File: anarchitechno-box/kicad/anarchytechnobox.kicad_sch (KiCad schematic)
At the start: 19 parts, among them J1 Conn_01x02, Q1 IRLZ44N, Q2 IRFS4310Z, U1 TC4426xOA, U2 ADuM1200AR, U4 LM7812_TO220, U5 L7805, U6 TME-0503S

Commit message: RP2350 initial commit
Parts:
- removed A1: RaspberryPi_Pico_W, Module:RaspberryPi_Pico_W_SMD_HandSolder, symbol MCU_Module:RaspberryPi_Pico_W
- removed D1, D4: D_Schottky, symbol Device:D_Schottky
- removed D2: RED, symbol Device:LED
- removed D5: GREEN, symbol Device:LED
- removed F1: Polyfuse, symbol Device:Polyfuse
- removed J1: Conn_01x02, symbol Connector_Generic:Conn_01x02
- removed Q1: IRLZ44N, Package_TO_SOT_THT:TO-220-3_Vertical, symbol Transistor_FET:IRLZ44N
- removed Q2: IRFS4310Z, Package_TO_SOT_SMD:TO-263-2, symbol Transistor_FET:IRFS4310Z
- removed R1: 2k2, symbol Device:R
- removed R2: 100R, symbol Device:R
- removed R3: 10k, symbol Device:R
- removed R4: 2k2, symbol Device:R_Small
- removed U1: TC4426xOA, Package_SO:SOIC-8_3.9x4.9mm_P1.27mm, symbol Driver_FET:TC4426xOA
- removed U2: ADuM1200AR, Package_SO:SOIC-8_3.9x4.9mm_P1.27mm, symbol Isolator:ADuM1200AR
- added C101, C102: 100nF, Capacitor_SMD:C_0402_1005Metric, symbol TINRS - Wobbler (pico)sch-eagle-import:C-EUC0402
- added D1, D101: C5349953, TinyLEDs:XL-1010, symbol TinyLEDs:XL-1010
- added H11, H12, H5, H7, H8, H9: MountingHole, MountingHole:MountingHole_3.2mm_M3, symbol Mechanical:MountingHole
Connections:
- net GND: now also C101.1, C102.1, D1.3 (GND), D101.3 (GND)
- new net: D1.1 (DO), D101.4 (DI)
- new net +3V3: C101.2, C102.2, D1.2 (VDD), D101.2 (VDD)
- new net LED_STRING: D1.4 (DI)
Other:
- added sheet RP2350BMCU (RP2350BMCU.kicad_sch)
- added sheet TwoIsolatedFETs (TwoIsolatedFETs.kicad_sch)
- added sheet TwoIsolatedFETs1 (TwoIsolatedFETs.kicad_sch)
- added sheet TwoIsolatedFETs2 (TwoIsolatedFETs.kicad_sch)
- added sheet TwoIsolatedFETs3 (TwoIsolatedFETs.kicad_sch)
- note removed: "both footprints possible: Dpak 252 or TO220"

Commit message: Large intermediate schematic push. Remaining todos are on frontpage.
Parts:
- renumbered C101 to C1, C102 to C2, D3 to D1, D1 to D2, D101 to D3, H5 to H1, H9 to H2, H7 to H3, H11 to H4, H12 to H5, H8 to H6, U6 to U1, U5 to U2, U4 to U3
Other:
- sheet TwoIsolatedFETs renamed TwoIsolatedFETs0
- removed sheet TwoIsolatedFETs2
- removed sheet TwoIsolatedFETs3
- added sheet DCDC Flyback (dcdc_flyback.kicad_sch)
- added sheet Ethernet (eth_w5500.kicad_sch)
- added sheet Isolators (isolators.kicad_sch)
- sheet RP2350BMCU ports: added DRV_CS1, DRV_CS2, DRV_CS3, DRV_CS4, DRV_MISO, DRV_MOSI, DRV_SCK, DRV_nFAULT, ETH_CS, ETH_MISO, ETH_MOSI, ETH_SCK, I2C0_SCL, I2C0_SDA, I2C1_SCL, I2C1_SDA, PMW1_A, PWM0_A, PWM10_A, PWM11_A, PWM2_A, PWM3_A, PWM4_A, PWM5_A, PWM6_A, PWM7_A, PWM8_A, PWM9_A, UART0_RX, UART0_TX, UART1_RX, UART1_TX; removed none
- sheet TwoIsolatedFETs0 ports: added DRV_nFAULT_COMMON, MCU_PWM_A_1, MCU_PWM_A_2, MCU_PWM_B_1, MCU_PWM_B_2, OUTPUT_A, OUTPUT_B, OUTPUT_C, OUTPUT_D, PWM_A_OFF, PWM_B_OFF, SPI_CLK, SPI_CS_A, SPI_CS_B, SPI_MISO, SPI_MOSI; removed Input_A, Input_B
- sheet TwoIsolatedFETs1 ports: added DRV_nFAULT_COMMON, MCU_PWM_A_1, MCU_PWM_A_2, MCU_PWM_B_1, MCU_PWM_B_2, OUTPUT_A, OUTPUT_B, OUTPUT_C, OUTPUT_D, PWM_A_OFF, PWM_B_OFF, SPI_CLK, SPI_CS_A, SPI_CS_B, SPI_MISO, SPI_MOSI; removed Input_A, Input_B
- note added: "HIGH POWER SIDE"
- note added: "MCU SIDE"
- note added: "TODO: - Add 3.3V regulator at power side (+3.3VP) - Add off-the-shelf isolated 5V 6W+ DC/DC (e.g. Recom REC10K-2405SAW/H2) - Add LED indicator chain (I moved Rpi pin) - does it need stay isolated? - Check if Pin allocations don't collide (in particular PWMs and SPIs) - MIDI stuff - OLED display connector - Optocoupler inputs - Rotary encoder etc. - Groove connector"
- moved on the sheet: C1, C2, D1, H1, H2, H3, H4, H5, H6, U1, U2, U3

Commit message: Stijn in de Trein
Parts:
- added J3, J4, J5, J6: Screw_Terminal_01x02, TerminalBlock_Phoenix:TerminalBlock_Phoenix_PT-1,5-2-5.0-H_1x02_P5.00mm_Horizontal, symbol Connector:Screw_Terminal_01x02
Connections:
- net TwoIsolatedFETs0/OUTPUT_A: now also J3.1 (Pin_1)
- net TwoIsolatedFETs0/OUTPUT_B: now also J3.2 (Pin_2)
- net TwoIsolatedFETs0/OUTPUT_C: now also J4.1 (Pin_1)
- net TwoIsolatedFETs0/OUTPUT_D: now also J4.2 (Pin_2)
- net TwoIsolatedFETs1/OUTPUT_A: now also J5.1 (Pin_1)
- net TwoIsolatedFETs1/OUTPUT_B: now also J5.2 (Pin_2)
- net TwoIsolatedFETs1/OUTPUT_C: now also J6.1 (Pin_1)
- net TwoIsolatedFETs1/OUTPUT_D: now also J6.2 (Pin_2)

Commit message: meer Stijn in de Trein
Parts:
- added C86, C87, C88, C89, C90, C91: 100nF, Capacitor_SMD:C_0402_1005Metric, symbol TINRS - Wobbler (pico)sch-eagle-import:C-EUC0402
- added D18, D19, D20, D21, D22, D23: C5349953, TinyLEDs:XL-1010, symbol TinyLEDs:XL-1010
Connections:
- net +3V3: now also C86.2, C87.2, C88.2, C89.2, C90.2, C91.2, D18.2 (VDD), D19.2 (VDD), D20.2 (VDD), D21.2 (VDD), D22.2 (VDD), D23.2 (VDD)
- net GND: now also C86.1, C87.1, C88.1, C89.1, C90.1, C91.1, D18.3 (GND), D19.3 (GND), D20.3 (GND), D21.3 (GND), D22.3 (GND), D23.3 (GND)
- net at D3.1 (DO): now also D18.4 (DI)
- net TwoIsolatedFETs0/OUTPUT_A renamed HB_1_OUT_A
- net TwoIsolatedFETs0/OUTPUT_B renamed HB_1_OUT_B
- net TwoIsolatedFETs0/OUTPUT_C renamed HB_1_OUT_C
- net TwoIsolatedFETs0/OUTPUT_D renamed HB_1_OUT_D
- net TwoIsolatedFETs1/OUTPUT_A renamed HB_2_OUT_A
- net TwoIsolatedFETs1/OUTPUT_B renamed HB_2_OUT_B
- net TwoIsolatedFETs1/OUTPUT_C renamed HB_2_OUT_C
- net TwoIsolatedFETs1/OUTPUT_D renamed HB_2_OUT_D
- new net: D22.1 (DO), D23.4 (DI)
- new net: D21.1 (DO), D22.4 (DI)
- new net: D20.1 (DO), D21.4 (DI)
- new net: D18.1 (DO), D19.4 (DI)
- new net: D19.1 (DO), D20.4 (DI)
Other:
- moved on the sheet: J3, J4, J5, J6

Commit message: nog meer trein
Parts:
- removed J3, J4, J5, J6: Screw_Terminal_01x02, TerminalBlock_Phoenix:TerminalBlock_Phoenix_PT-1,5-2-5.0-H_1x02_P5.00mm_Horizontal, symbol Connector:Screw_Terminal_01x02
- added J3, J4, J5, J6: Screw_Terminal_01x03, TerminalBlock_Phoenix:TerminalBlock_Phoenix_MKDS-1,5-3-5.08_1x03_P5.08mm_Horizontal, symbol Connector:Screw_Terminal_01x03
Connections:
- net GND2: now also J3.2 (Pin_2), J4.2 (Pin_2), J5.2 (Pin_2), J6.2 (Pin_2)
- net HB_1_OUT_A: now also J3.1 (Pin_1)
- net HB_1_OUT_B: now also J3.3 (Pin_3)
- net HB_1_OUT_C: now also J4.1 (Pin_1)
- net HB_1_OUT_D: now also J4.3 (Pin_3)
- net HB_2_OUT_A: now also J5.1 (Pin_1)
- net HB_2_OUT_B: now also J5.3 (Pin_3)
- net HB_2_OUT_C: now also J6.1 (Pin_1)
- net HB_2_OUT_D: now also J6.3 (Pin_3)

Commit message: trein trein trein
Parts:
- removed D1: SM6T24A, Diode_SMD:D_SMB, symbol Diode:SM6T24A
- removed U1: TME-0503S, Converter_DCDC:Converter_DCDC_TRACO_TME_03xxS_05xxS_12xxS_Single_THT, symbol Converter_DCDC:TME-0503S
- removed U2: L7805, symbol Regulator_Linear:L7805
- removed U3: LM7812_TO220, Package_TO_SOT_THT:TO-220-3_Vertical, symbol Regulator_Linear:LM7812_TO220

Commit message: choo choooooo
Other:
- added sheet RS485 (RS485.kicad_sch)
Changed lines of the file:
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@@
 		)
 	)
+	(wire
+		(pts
+			(xy 91.44 88.9) (xy 99.06 88.9)
+		)
+		(stroke
+			(width 0)
+			(type default)
+		)
+	)
 	(polyline
 		(pts
@@
 	(wire
 		(pts
+			(xy 91.44 86.36) (xy 99.06 86.36)
+		)
+		(stroke
+			(width 0)
+			(type default)
+		)
+	)
+	(wire
+		(pts
 			(xy 238.76 123.19) (xy 294.64 123.19)
 		)
@@
 				)
 			)
+		)
+	)
+	(sheet
+		(at 69.85 78.74)
+		(size 21.59 12.7)
+		(exclude_from_sim no)
+		(in_bom yes)
+		(on_board yes)
+		(dnp no)
+		(fields_autoplaced yes)
+		(stroke
+			(width 0.1524)
+			(type solid)
+		)
+		(fill
+			(color 0 0 0 0.0000)
+		)
+		(property "Sheetname" "RS485"
+			(at 69.85 78.0284 0)
+			(effects
+				(font
+					(size 1.27 1.27)
+				)
+				(justify left bottom)
+			)
+		)
+		(property "Sheetfile" "RS485.kicad_sch"
+			(at 69.85 92.0246 0)
+			(effects
+				(font
+					(size 1.27 1.27)
+				)
+				(justify left top)
+				(hide yes)
+			)
+		)
+		(pin "485_~{RE}" input
+			(at 69.85 82.55 180)
+			(effects
+				(font
+					(size 1.27 1.27)
+				)
+				(justify left)
+			)
+		)
+		(pin "FROM_RS485" output
+			(at 91.44 88.9 0)
+			(effects
+				(font
+					(size 1.27 1.27)
+				)
+				(justify right)
+			)
+		)
+		(pin "485_DE" input
+			(at 69.85 85.09 180)
+			(effects
+				(font
+					(size 1.27 1.27)
+				)
+				(justify left)
+			)
+		)
+		(pin "TO_RS485" input
+			(at 91.44 86.36 0)
+			(effects
+				(font
+					(size 1.27 1.27)
+				)
+				(justify right)
+			)
+		)
+		(instances
+			(project "anarchytechnobox"
+				(path "/8c734c41-38ed-40fc-83bd-134786dcfb35"
+					(page "12")
+				)
+			)

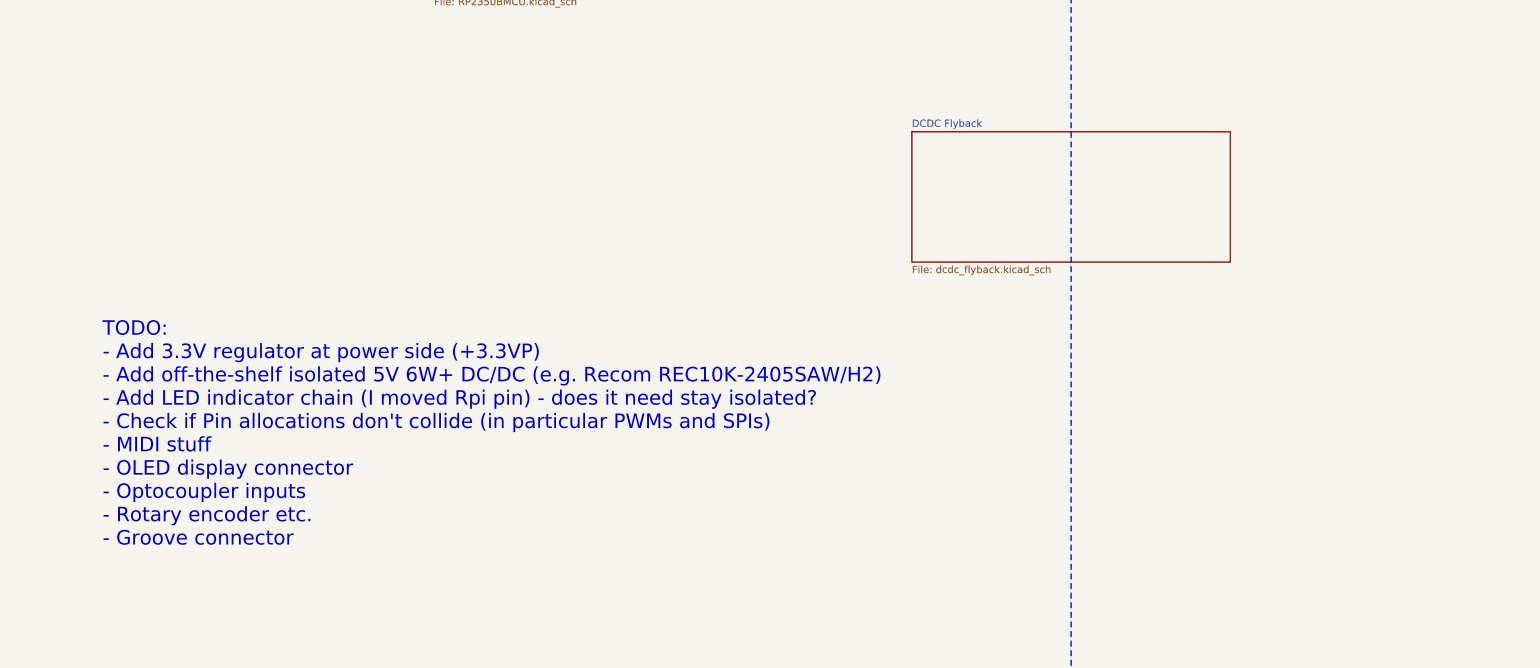
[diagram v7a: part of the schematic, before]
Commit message: Resized PCB with mounts at 125x125mm (suitable for 140mm PC fan), 4-pin fan connector added, changed 3.3VP to 5.0VP
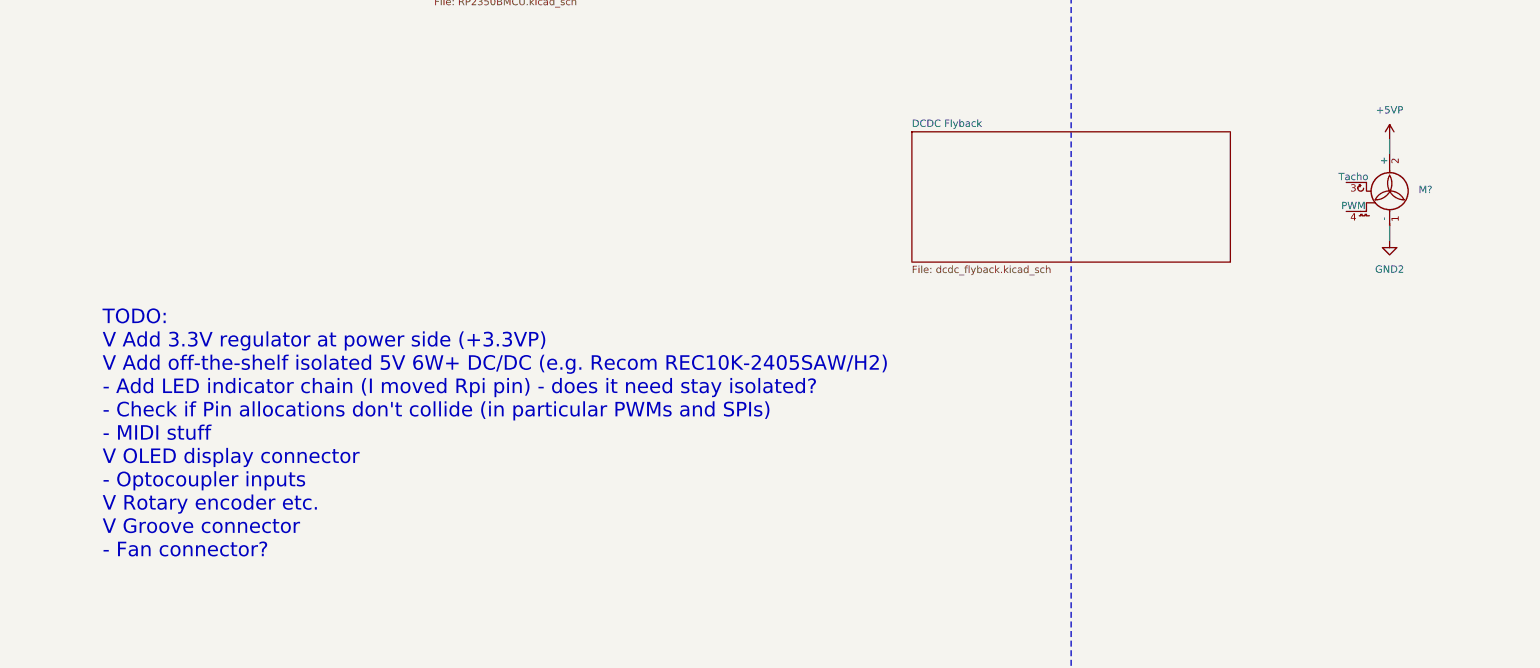
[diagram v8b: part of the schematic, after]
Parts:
- added M?: Fan_Tacho_PWM, Connector:FanPinHeader_1x04_P2.54mm_Vertical, symbol Motor:Fan_Tacho_PWM
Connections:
- net GND2: now also M?.1 (-)
- new net +5VP: M?.2 (+)
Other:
- note added: "TODO: V Add 3.3V regulator at power side (+3.3VP) V Add off-the-shelf isolated 5V 6W+ DC/DC (e.g. Recom REC10K-2405SAW/H2) - Add LED indicator chain (I moved Rpi pin) - does it need stay isolated? - Check if Pin allocations don't collide (in particular PWMs and SPIs) - MIDI stuff V OLED display connector - Optocoupler inputs V Rotary encoder etc. V Groove connector - Fan connector?"
- note removed: "TODO: - Add 3.3V regulator at power side (+3.3VP) - Add off-the-shelf isolated 5V 6W+ DC/DC (e.g. Recom REC10K-2405SAW/H2) - Add LED indicator chain (I moved Rpi pin) - does it need stay isolated? - Check if Pin allocations don't collide (in particular PWMs and SPIs) - MIDI stuff - OLED display connector - Optocoupler inputs - Rotary encoder etc. - Groove connector"
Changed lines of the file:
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@@
 		)
 	)
-	(text "TODO:\n- Add 3.3V regulator at power side (+3.3VP)\n- Add off-the-shelf isolated 5V 6W+ DC/DC (e.g. Recom REC10K-2405SAW/H2)\n- Add LED indicator chain (I moved Rpi pin) - does it need stay isolated?\n- Check if Pin allocations don't collide (in particular PWMs and SPIs)\n- MIDI stuff\n- OLED display connector\n- Optocoupler inputs\n- Rotary encoder etc.\n- Groove connector"
+	(text "TODO:\nV Add 3.3V regulator at power side (+3.3VP)\nV Add off-the-shelf isolated 5V 6W+ DC/DC (e.g. Recom REC10K-2405SAW/H2)\n- Add LED indicator chain (I moved Rpi pin) - does it need stay isolated?\n- Check if Pin allocations don't collide (in particular PWMs and SPIs)\n- MIDI stuff\nV OLED display connector\n- Optocoupler inputs\nV Rotary encoder etc.\nV Groove connector\n- Fan connector?"
 		(exclude_from_sim no)
 		(at 40.894 233.426 0)
@@
 	(wire
 		(pts
+			(xy 266.7 199.39) (xy 266.7 196.85)
+		)
+		(stroke
+			(width 0)
+			(type default)
+		)
+	)
+	(wire
+		(pts
 			(xy 68.58 135.89) (xy 99.06 135.89)
 		)
@@
 		)
 	)
+	(wire
+		(pts
+			(xy 266.7 181.61) (xy 266.7 184.15)
+		)
+		(stroke
+			(width 0)
+			(type default)
+		)
+	)
 	(polyline
 		(pts
@@
 	)
 	(symbol
+		(lib_id "power:GND2")
+		(at 266.7 199.39 0)
+		(unit 1)
+		(exclude_from_sim no)
+		(in_bom yes)
+		(on_board yes)
+		(dnp no)
+		(fields_autoplaced yes)
+		(property "Reference" "#PWR0135"
+			(at 266.7 205.74 0)
+			(effects
+				(font
+					(size 1.27 1.27)
+				)
+				(hide yes)
+			)
+		)
+		(property "Value" "GND2"
+			(at 266.7 204.47 0)
+			(effects
+				(font
+					(size 1.27 1.27)
+				)
+			)
+		)
+		(property "Footprint" ""
+			(at 266.7 199.39 0)
+			(effects
+				(font
+					(size 1.27 1.27)
+				)
+				(hide yes)
+			)
+		)
+		(property "Datasheet" ""
+			(at 266.7 199.39 0)
+			(effects
+				(font
+					(size 1.27 1.27)
+				)
+				(hide yes)
+			)
+		)
+		(property "Description" "Power symbol creates a global label with name \"GND2\" , ground"
+			(at 266.7 199.39 0)
+			(effects
+				(font
+					(size 1.27 1.27)
+				)
+				(hide yes)
+			)
+		)
+		(pin "1"
+		)
+		(instances
+			(project "anarchytechnobox"
+				(path "/8c734c41-38ed-40fc-83bd-134786dcfb35"
+					(reference "#PWR0135")
+					(unit 1)
+				)
+			)
+		)
+	)
+	(symbol
+		(lib_id "power:+5VP")
+		(at 266.7 181.61 0)
+		(unit 1)
+		(exclude_from_sim no)
+		(in_bom yes)
+		(on_board yes)
+		(dnp no)
+		(fields_autoplaced yes)
+		(property "Reference" "#PWR0117"
+			(at 266.7 185.42 0)
+			(effects
+				(font
+					(size 1.27 1.27)
+				)
+				(hide yes)
+			)
+		)
+		(property "Value" "+5VP"
+			(at 266.7 176.53 0)
+			(effects
+				(font
+					(size 1.27 1.27)
+				)
+			)
+		)
+		(property "Footprint" ""
+			(at 266.7 181.61 0)
+			(effects
+				(font
+					(size 1.27 1.27)
+				)
+				(hide yes)
+			)
+		)
+		(property "Datasheet" ""
+			(at 266.7 181.61 0)
+			(effects
+				(font
+					(size 1.27 1.27)
+				)
+				(hide yes)
+			)
+		)
+		(property "Description" "Power symbol creates a global label with name \"+5VP\""
+			(at 266.7 181.61 0)
+			(effects
+				(font
+					(size 1.27 1.27)
+				)
+				(hide yes)
+			)
+		)
+		(pin "1"
+		)
+		(instances
+			(project "anarchytechnobox"
+				(path "/8c734c41-38ed-40fc-83bd-134786dcfb35"
+					(reference "#PWR0117")
+					(unit 1)
+				)
+			)
+		)
+	)
+	(symbol
 		(lib_id "Mechanical:MountingHole")
 		(at 17.78 19.05 0)
@@
 					(unit 1)
 				)
+			)
+		)
+	)
+	(symbol
+		(lib_id "Motor:Fan_Tacho_PWM")
+		(at 266.7 191.77 0)
+		(unit 1)
+		(exclude_from_sim no)
+		(in_bom yes)
+		(on_board yes)
+		(dnp no)
+		(fields_autoplaced yes)
+		(property "Reference" "M?"
+			(at 271.78 190.4999 0)
+			(effects
+				(font
+					(size 1.27 1.27)
+				)
+				(justify left)
+			)
+		)
+		(property "Value" "Fan_Tacho_PWM"
+			(at 271.78 193.0399 0)
+			(effects
+				(font
+					(size 1.27 1.27)
+				)
+				(justify left)
+				(hide yes)
+			)
+		)
+		(property "Footprint" "Connector:FanPinHeader_1x04_P2.54mm_Vertical"
+			(at 266.7 191.516 0)
+			(effects
+				(font
+					(size 1.27 1.27)
+				)
+				(hide yes)
+			)
+		)
+		(property "Datasheet" "http://www.formfactors.org/developer%5Cspecs%5Crev1_2_public.pdf"
+			(at 266.7 191.516 0)
+			(effects
+				(font
+					(size 1.27 1.27)
+				)
+				(hide yes)
+			)
+		)
+		(property "Description" "Fan, tacho output, PWM input, 4-pin connector"
+			(at 266.7 191.77 0)
+			(effects
+				(font
+					(size 1.27 1.27)
+				)
+				(hide yes)
+			)
+		)
+		(pin "1"
+		)
+		(pin "3"
+		)
+		(pin "4"
+		)
+		(pin "2"
+		)
+		(instances
+			(project "anarchytechnobox"
+				(path "/8c734c41-38ed-40fc-83bd-134786dcfb35"
+					(reference "M?")
+					(unit 1)
+				)
